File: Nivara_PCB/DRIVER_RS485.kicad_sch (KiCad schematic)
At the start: 7 parts, among them U3 RSM3485ECHT_C2992406

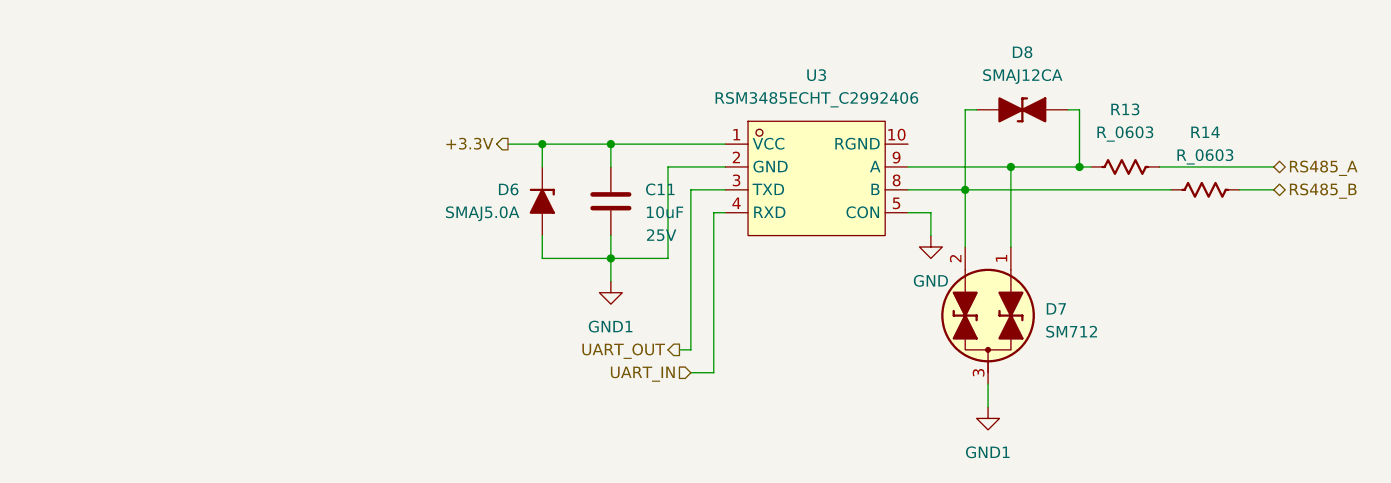
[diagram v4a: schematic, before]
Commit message: Cambios realizados en el PCB y el esquema de Nivara_PCB.
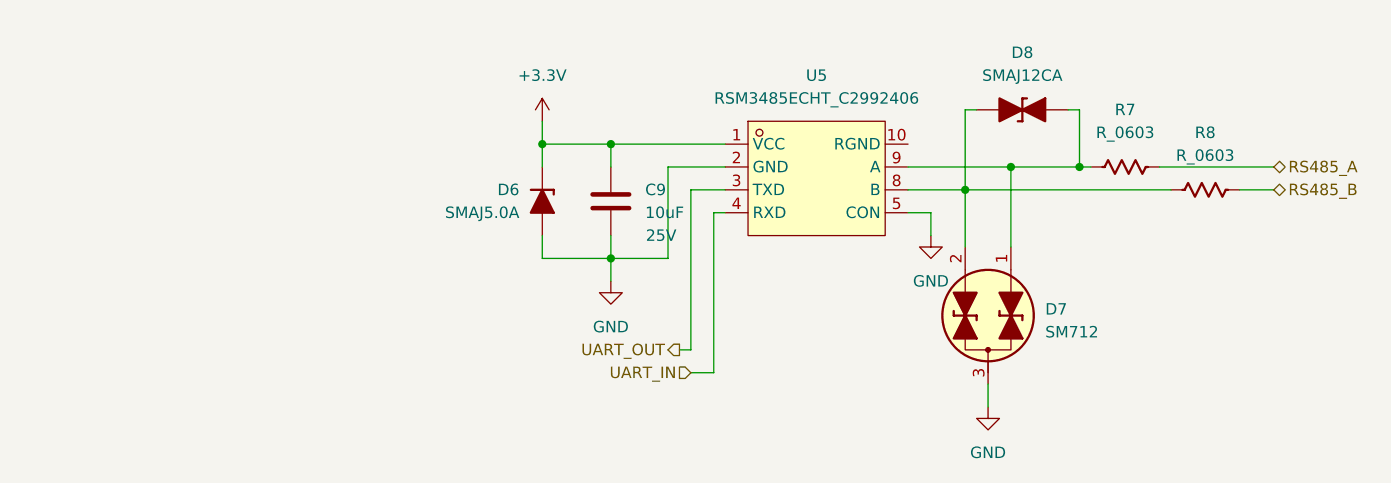
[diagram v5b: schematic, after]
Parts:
- renumbered C11 to C9, R13 to R7, R14 to R8, U3 to U5
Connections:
- net GND1 is gone; now on net GND: C9.2, D6.2 (A), D7.3 (Com), U5.2 (GND)
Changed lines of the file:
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@@
-	(wire
-		(pts
-			(xy 73.66 62.23) (xy 77.47 62.23)
-		)
-		(stroke
-			(width 0)
-			(type default)
-		)
-	)
 	(wire
 		(pts
@@
 	(wire
 		(pts
+			(xy 77.47 59.69) (xy 77.47 62.23)
+		)
+		(stroke
+			(width 0)
+			(type default)
+		)
+	)
+	(wire
+		(pts
 			(xy 135.89 58.42) (xy 137.16 58.42)
 		)
@@
 			(width 0)
 			(type default)
-		)
-	)
-	(hierarchical_label "+3.3V"
-		(shape output)
-		(at 73.66 62.23 180)
-		(effects
-			(font
-				(size 1.27 1.27)
-			)
-			(justify right)
 		)
 	)
@@
 		(on_board yes)
 		(dnp no)
-		(property "Reference" "C11"
+		(property "Reference" "C9"
 			(at 88.9 67.3099 0)
 			(effects
@@
 			(project "Nivara_PCB"
 				(path "/13184db0-a71d-4054-b13a-bbf46d2b100d/4e7fa7f2-8bf5-4f9c-874d-fa1b4fd76f92/3eeaffcc-9bb5-4f36-a3b6-9bf8c04eaeb0"
-					(reference "C11")
+					(reference "C9")
+					(unit 1)
+				)
+			)
+		)
+	)
+	(symbol
+		(lib_id "power:GND")
+		(at 127 91.44 0)
+		(unit 1)
+		(exclude_from_sim no)
+		(in_bom yes)
+		(on_board yes)
+		(dnp no)
+		(fields_autoplaced yes)
+		(property "Reference" "#PWR025"
+			(at 127 97.79 0)
+			(effects
+				(font
+					(size 1.27 1.27)
+				)
+				(hide yes)
+			)
+		)
+		(property "Value" "GND"
+			(at 127 96.52 0)
+			(effects
+				(font
+					(size 1.27 1.27)
+				)
+			)
+		)
+		(property "Footprint" ""
+			(at 127 91.44 0)
+			(effects
+				(font
+					(size 1.27 1.27)
+				)
+				(hide yes)
+			)
+		)
+		(property "Datasheet" ""
+			(at 127 91.44 0)
+			(effects
+				(font
+					(size 1.27 1.27)
+				)
+				(hide yes)
+			)
+		)
+		(property "Description" "Power symbol creates a global label with name \"GND\" , ground"
+			(at 127 91.44 0)
+			(effects
+				(font
+					(size 1.27 1.27)
+				)
+				(hide yes)
+			)
+		)
+		(pin "1"
+		)
+		(instances
+			(project "Nivara_PCB"
+				(path "/13184db0-a71d-4054-b13a-bbf46d2b100d/4e7fa7f2-8bf5-4f9c-874d-fa1b4fd76f92/3eeaffcc-9bb5-4f36-a3b6-9bf8c04eaeb0"
+					(reference "#PWR025")
 					(unit 1)
 				)
@@
 		(dnp no)
 		(fields_autoplaced yes)
-		(property "Reference" "R13"
+		(property "Reference" "R7"
 			(at 142.24 58.42 90)
 			(effects
@@
 			(project ""
 				(path "/13184db0-a71d-4054-b13a-bbf46d2b100d/4e7fa7f2-8bf5-4f9c-874d-fa1b4fd76f92/3eeaffcc-9bb5-4f36-a3b6-9bf8c04eaeb0"
-					(reference "R13")
+					(reference "R7")
 					(unit 1)
 				)
@@
 		(dnp no)
 		(fields_autoplaced yes)
-		(property "Reference" "#PWR045"
+		(property "Reference" "#PWR023"
 			(at 85.09 83.82 0)
 			(effects
@@
 			)
 		)
-		(property "Value" "GND1"
+		(property "Value" "GND"
 			(at 85.09 82.55 0)
 			(effects
@@
 			(project "Nivara_PCB"
 				(path "/13184db0-a71d-4054-b13a-bbf46d2b100d/4e7fa7f2-8bf5-4f9c-874d-fa1b4fd76f92/3eeaffcc-9bb5-4f36-a3b6-9bf8c04eaeb0"
-					(reference "#PWR045")
+					(reference "#PWR023")
 					(unit 1)
 				)
@@
 		(dnp no)
 		(fields_autoplaced yes)
-		(property "Reference" "U3"
+		(property "Reference" "U5"
 			(at 107.95 54.61 0)
 			(effects
@@
 			(project ""
 				(path "/13184db0-a71d-4054-b13a-bbf46d2b100d/4e7fa7f2-8bf5-4f9c-874d-fa1b4fd76f92/3eeaffcc-9bb5-4f36-a3b6-9bf8c04eaeb0"
-					(reference "U3")
+					(reference "U5")
 					(unit 1)
 				)
@@
 		(dnp no)
 		(fields_autoplaced yes)
-		(property "Reference" "R14"
+		(property "Reference" "R8"
 			(at 151.13 60.96 90)
 			(effects
@@
 			(project "Nivara_PCB"
 				(path "/13184db0-a71d-4054-b13a-bbf46d2b100d/4e7fa7f2-8bf5-4f9c-874d-fa1b4fd76f92/3eeaffcc-9bb5-4f36-a3b6-9bf8c04eaeb0"
-					(reference "R14")
-					(unit 1)
-				)
-			)
-		)
-	)
-	(symbol
-		(lib_id "power:GND")
-		(at 127 91.44 0)
+					(reference "R8")
+					(unit 1)
+				)
+			)
+		)
+	)
+	(symbol
+		(lib_id "power:+3.3V")
+		(at 77.47 59.69 0)
 		(unit 1)
 		(exclude_from_sim no)
@@
 		(dnp no)
 		(fields_autoplaced yes)
-		(property "Reference" "#PWR047"
-			(at 127 97.79 0)
-			(effects
-				(font
-					(size 1.27 1.27)
-				)
-				(hide yes)
-			)
-		)
-		(property "Value" "GND1"
-			(at 127 96.52 0)
+		(property "Reference" "#PWR022"
+			(at 77.47 63.5 0)
+			(effects
+				(font
+					(size 1.27 1.27)
+				)
+				(hide yes)
+			)
+		)
+		(property "Value" "+3.3V"
+			(at 77.47 54.61 0)
 			(effects
 				(font
@@
 		)
 		(property "Footprint" ""
-			(at 127 91.44 0)
+			(at 77.47 59.69 0)
 			(effects
 				(font
@@
 		)
 		(property "Datasheet" ""
-			(at 127 91.44 0)
-			(effects
-				(font
-					(size 1.27 1.27)
-				)
-				(hide yes)
-			)
-		)
-		(property "Description" "Power symbol creates a global label with name \"GND\" , ground"
-			(at 127 91.44 0)
+			(at 77.47 59.69 0)
+			(effects
+				(font
+					(size 1.27 1.27)
+				)
+				(hide yes)
+			)
+		)
+		(property "Description" "Power symbol creates a global label with name \"+3.3V\""
+			(at 77.47 59.69 0)
 			(effects
 				(font
@@
 			(project "Nivara_PCB"
 				(path "/13184db0-a71d-4054-b13a-bbf46d2b100d/4e7fa7f2-8bf5-4f9c-874d-fa1b4fd76f92/3eeaffcc-9bb5-4f36-a3b6-9bf8c04eaeb0"
-					(reference "#PWR047")
+					(reference "#PWR022")
 					(unit 1)
 				)
@@
 		(dnp no)
 		(fields_autoplaced yes)
-		(property "Reference" "#PWR046"
+		(property "Reference" "#PWR024"
 			(at 120.65 78.74 0)
 			(effects
@@
 			(project "Nivara_PCB"
 				(path "/13184db0-a71d-4054-b13a-bbf46d2b100d/4e7fa7f2-8bf5-4f9c-874d-fa1b4fd76f92/3eeaffcc-9bb5-4f36-a3b6-9bf8c04eaeb0"
-					(reference "#PWR046")
-					(unit 1)
-				)
+					(reference "#PWR024")
+					(unit 1)
+				)

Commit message: Cambios realizados en los archivos de Nivara_PCB.
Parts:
- C9: symbol PCM_Capacitor_US_AKL:C_0603 -> EasyEDA:C_0603
- D6: symbol PCM_Diode_TVS_AKL:SMAJ5.0A -> EasyEDA:SMAJ5.0A
- D7: symbol PCM_Diode_TVS_AKL:SM712 -> EasyEDA:SM712
- D8: symbol PCM_Diode_TVS_AKL:SMAJ12CA -> EasyEDA:SMAJ12CA
- R7, R8: symbol PCM_Resistor_US_AKL:R_0603 -> EasyEDA:R_0603
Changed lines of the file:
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@@
 	)
 	(symbol
-		(lib_id "PCM_Capacitor_US_AKL:C_0603")
+		(lib_id "EasyEDA:C_0603")
 		(at 85.09 68.58 0)
 		(unit 1)
@@
 	)
 	(symbol
-		(lib_id "power:GND")
+		(lib_id "EasyEDA:GND")
 		(at 127 91.44 0)
 		(unit 1)
@@
 	)
 	(symbol
-		(lib_id "PCM_Diode_TVS_AKL:SMAJ5.0A")
+		(lib_id "EasyEDA:SMAJ5.0A")
 		(at 77.47 68.58 270)
 		(mirror x)
@@
 	)
 	(symbol
-		(lib_id "PCM_Diode_TVS_AKL:SM712")
+		(lib_id "EasyEDA:SM712")
 		(at 127 81.28 90)
 		(unit 1)
@@
 	)
 	(symbol
-		(lib_id "PCM_Resistor_US_AKL:R_0603")
+		(lib_id "EasyEDA:R_0603")
 		(at 142.24 64.77 90)
 		(unit 1)
@@
 	)
 	(symbol
-		(lib_id "PCM_Diode_TVS_AKL:SMAJ12CA")
+		(lib_id "EasyEDA:SMAJ12CA")
 		(at 130.81 58.42 0)
 		(unit 1)
@@
 	)
 	(symbol
-		(lib_id "power:GND")
+		(lib_id "EasyEDA:GND")
 		(at 85.09 77.47 0)
 		(unit 1)
@@
 	)
 	(symbol
-		(lib_id "PCM_Resistor_US_AKL:R_0603")
+		(lib_id "EasyEDA:R_0603")
 		(at 151.13 67.31 90)
 		(unit 1)
@@
 	)
 	(symbol
-		(lib_id "power:+3.3V")
+		(lib_id "EasyEDA:+3.3V")
 		(at 77.47 59.69 0)
 		(unit 1)
@@
 	)
 	(symbol
-		(lib_id "power:GND")
+		(lib_id "EasyEDA:GND")
 		(at 120.65 72.39 0)
 		(unit 1)
